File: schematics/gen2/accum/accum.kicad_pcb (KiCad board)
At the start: 2 copper layers, 100 x 91.1 mm, 16 parts, among them U1 74LS574, U2 74LS138, U3 74LS02, U4 74LS245, U5 74LS245, U6 74LS245

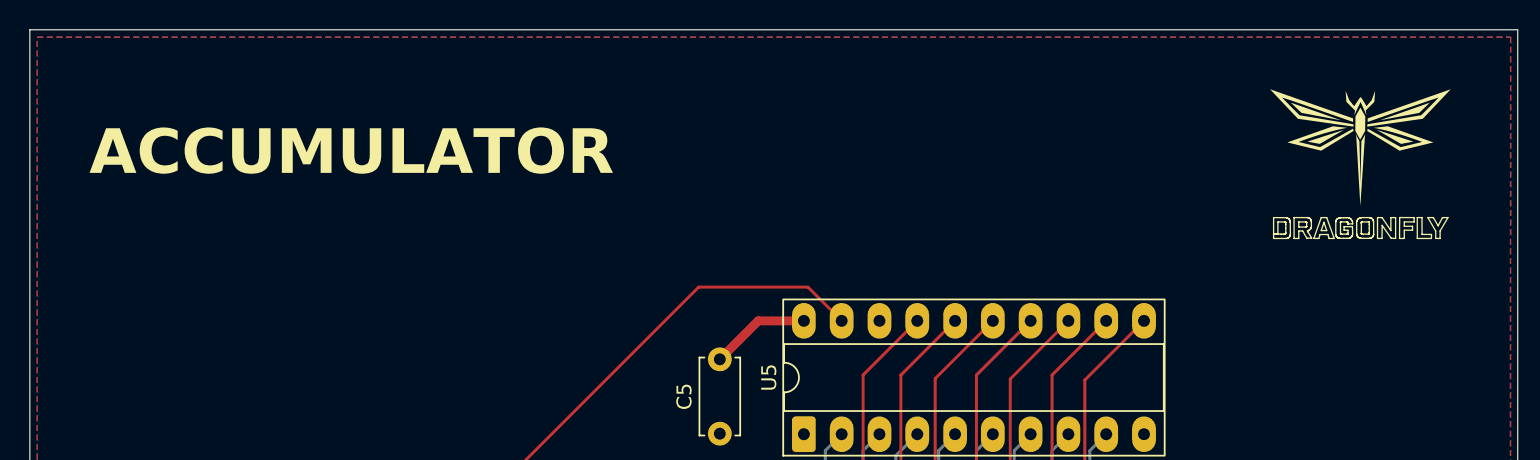
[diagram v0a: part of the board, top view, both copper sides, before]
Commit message: chore(accum): changed logo and text
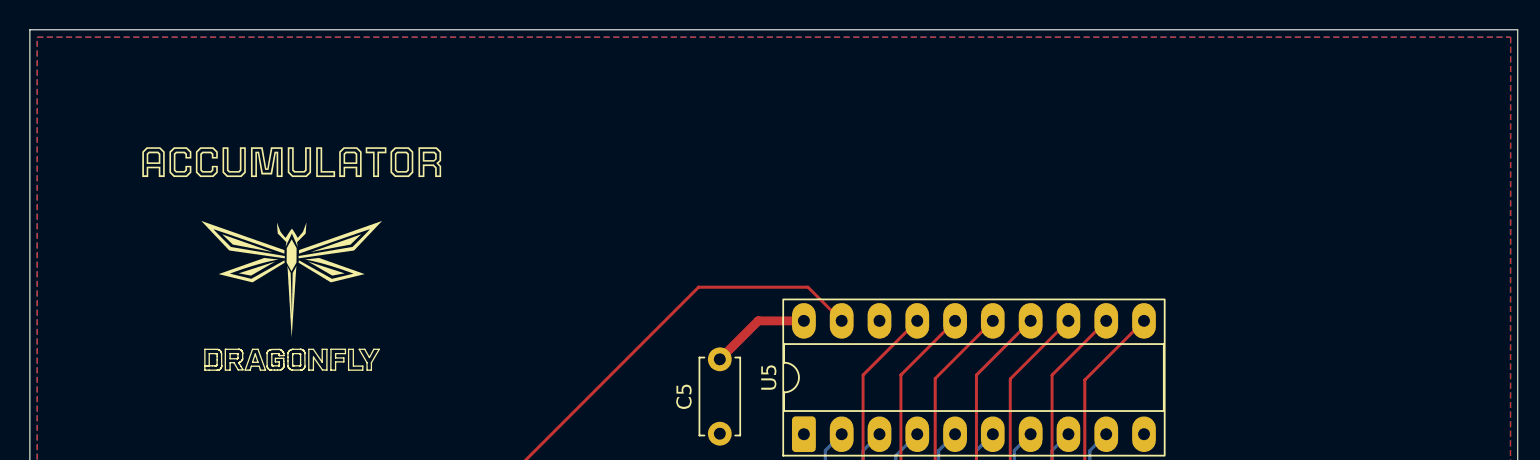
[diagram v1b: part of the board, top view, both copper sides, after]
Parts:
- added kibuzzard-6911C8C8: G***, kibuzzard-6911C8C8, F.Cu at (117.6, 58.4)
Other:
- board text removed: "ACCUMULATOR"

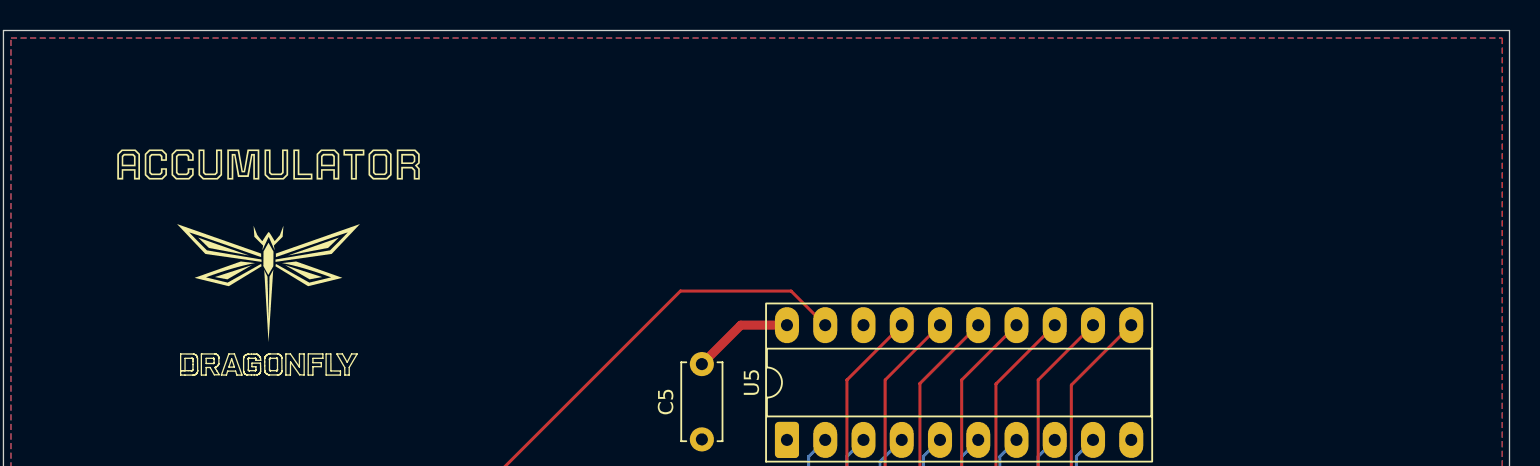
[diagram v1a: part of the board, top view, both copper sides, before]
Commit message: chore(kicad-pcb): added apps ucu logo
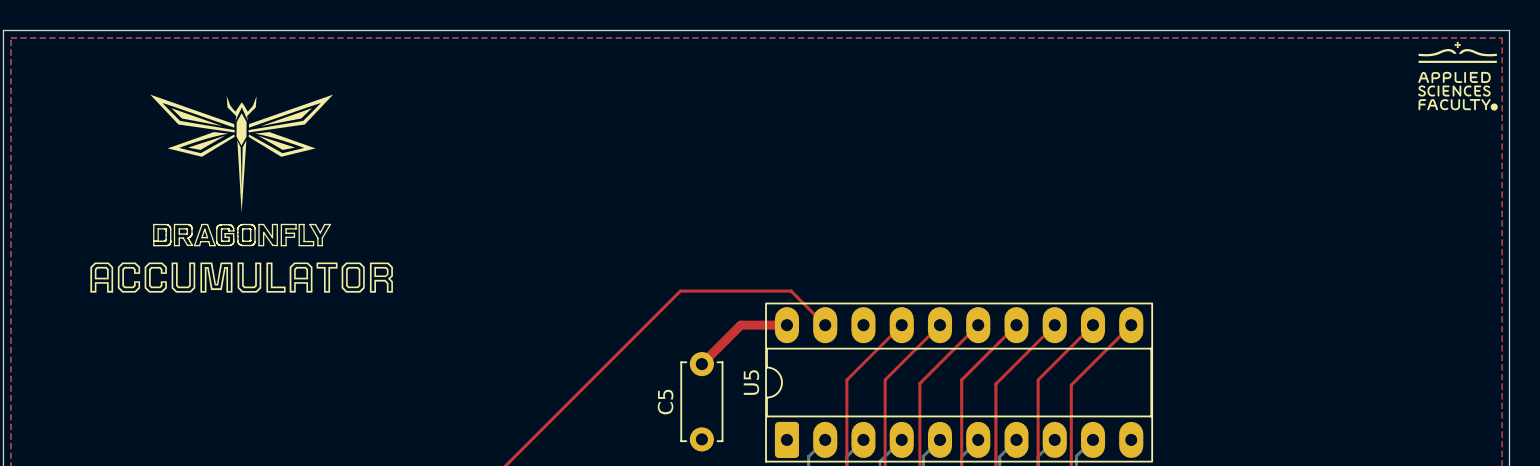
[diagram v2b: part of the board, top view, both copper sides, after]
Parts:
- moved kibuzzard-6911C8C8 7.72 mm to (115.8, 65.9)

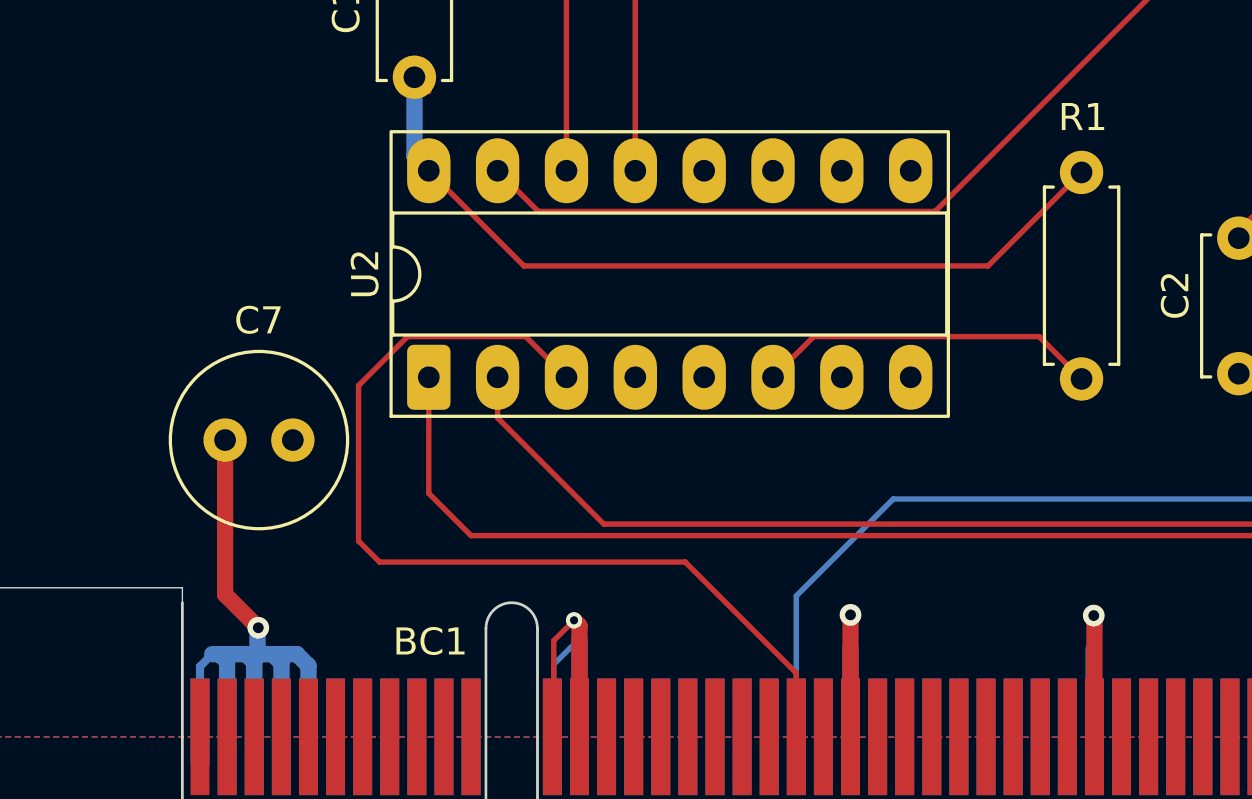
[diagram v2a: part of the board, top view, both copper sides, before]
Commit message: fix(kicad): vcc zones
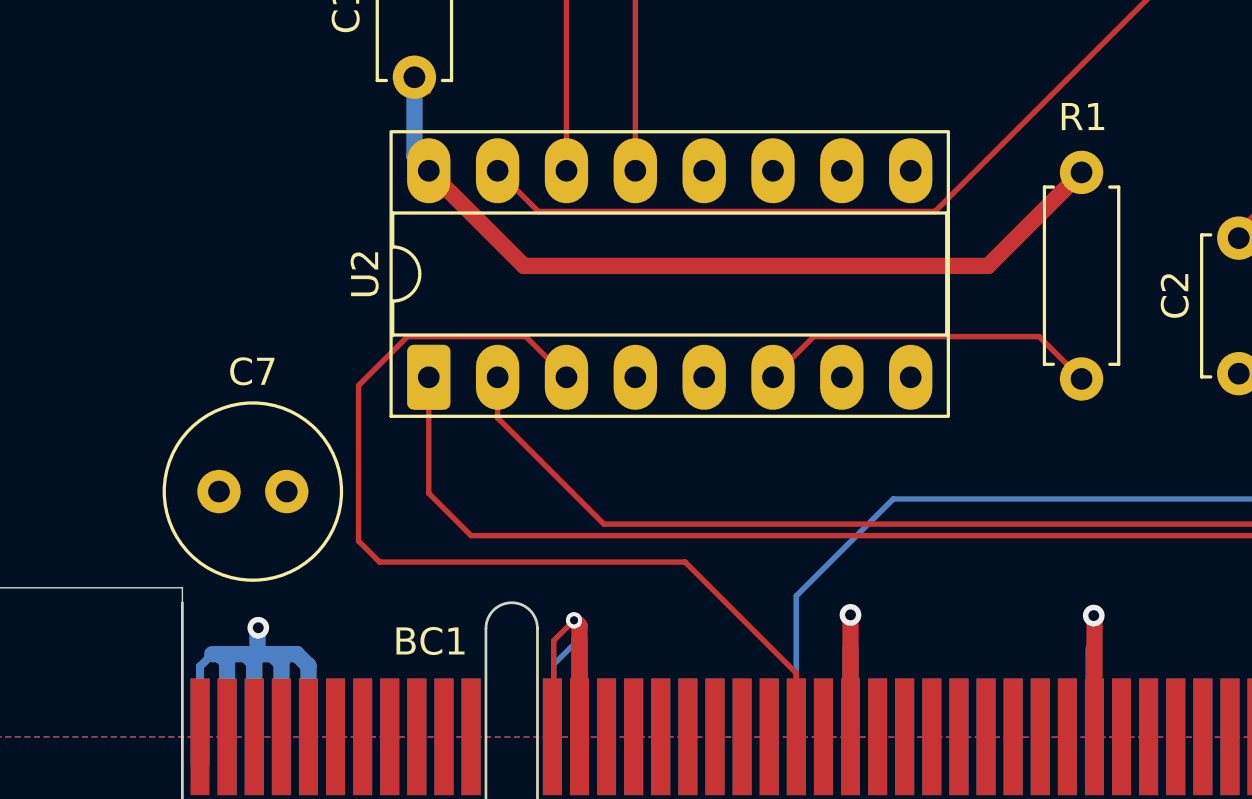
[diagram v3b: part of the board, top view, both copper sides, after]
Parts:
- moved C7 1.91 mm to (108.7, 136.4)
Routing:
- net VCC: track 114.3 -> 106.9 mm
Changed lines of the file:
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@@
 			(pinfunction "VCC")
 			(pintype "power_in")
+			(zone_connect 0)
 		)
 		(embedded_fonts no)
@@
 			(pinfunction "VCC")
 			(pintype "power_in")
+			(zone_connect 0)
 		)
 		(embedded_fonts no)
@@
 			(pinfunction "VCC")
 			(pintype "power_in")
+			(zone_connect 0)
 		)
 		(embedded_fonts no)
@@
 			(pinfunction "VCC")
 			(pintype "power_in")
+			(zone_connect 0)
 		)
 		(embedded_fonts no)
@@
 			(pinfunction "VCC")
 			(pintype "power_in")
+			(zone_connect 0)
 		)
 		(embedded_fonts no)
@@
 			(pinfunction "VCC")
 			(pintype "power_in")
+			(zone_connect 0)
 		)
 		(embedded_fonts no)
@@
 	(footprint "Capacitor_THT:C_Radial_D6.3mm_H5.0mm_P2.50mm"
 		(layer "F.Cu")
-		(at 108.925 134.55)
+		(at 108.7 136.45)
 		(descr "C, Radial series, Radial, pin pitch=2.50mm, diameter=6.3mm, height=5mm, Non-Polar Electrolytic Capacitor")
 		(tags "C Radial series Radial pin pitch 2.50mm diameter 6.3mm height 5mm Non-Polar Electrolytic Capacitor")
@@
 		(start 137.075 128.125)
 		(end 119.951666 128.125)
-		(width 0.2)
+		(width 0.6)
 		(layer "F.Cu")
 		(net 2)
@@
 		(start 140.525 124.675)
 		(end 137.075 128.125)
-		(width 0.2)
+		(width 0.6)
 		(layer "F.Cu")
 		(net 2)
@@
 		(start 119.951666 128.125)
 		(end 116.44 124.613334)
-		(width 0.2)
+		(width 0.6)
 		(layer "F.Cu")
 		(net 2)
@@
 	)
 	(segment
-		(start 110.15 141.475)
-		(end 108.925 140.25)
-		(width 0.6)
-		(layer "F.Cu")
-		(net 2)
-	)
-	(segment
 		(start 148.895 124.53)
 		(end 146.325 127.1)
@@
 		(width 0.6)
 		(layer "F.Cu")
-		(net 2)
-	)
-	(segment
-		(start 108.925 140.25)
-		(end 108.925 134.55)
-		(width 0.6)
-		(layer "F.Cu")
